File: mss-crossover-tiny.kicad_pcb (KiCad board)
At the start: 2 copper layers, 68.8 x 51 mm, 38 parts, among them J1 RJ45, J2 RJ45, J3 2x-screw, J4 2x-screw, J5 2x-screw, J6 ISP (5V), J7 2x-screw, Q1 2N3904, Q2 2N3904, SW1 Set, U1 L78M05CDT, U3 ATtiny25-20SS, U5 INA180A3

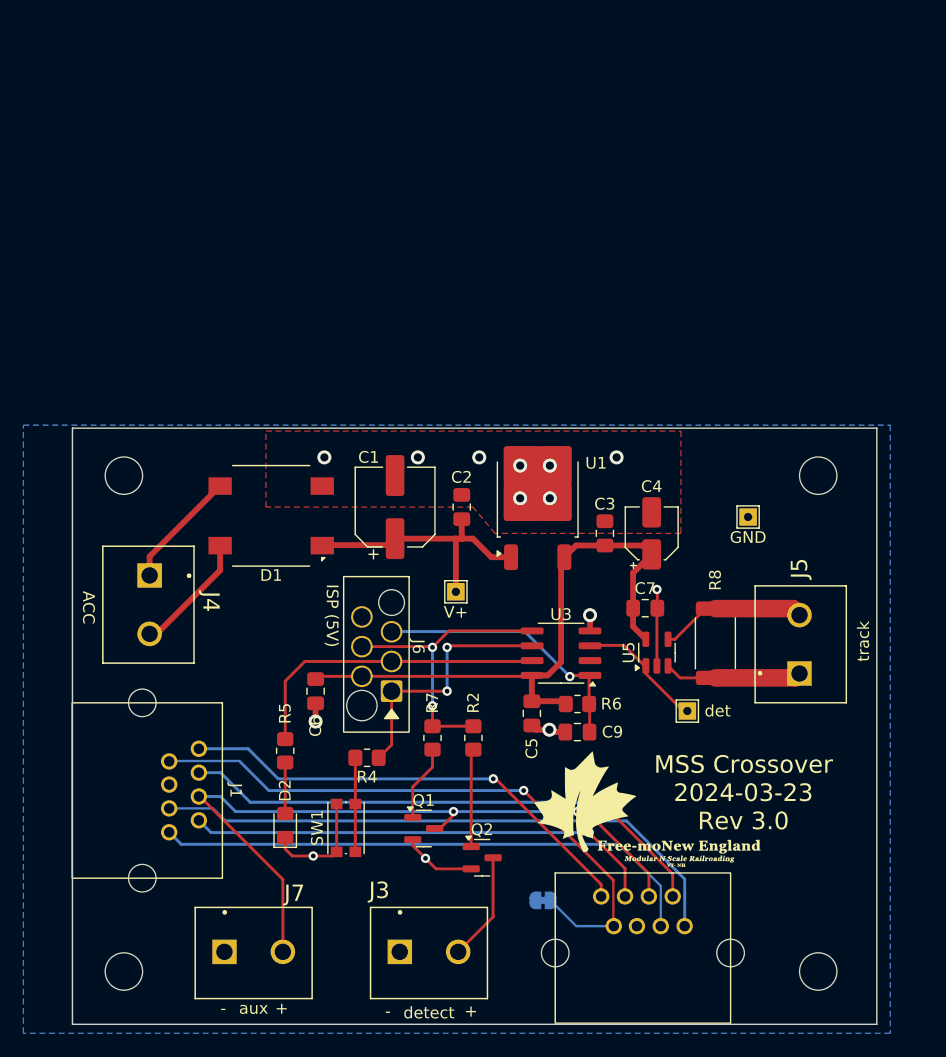
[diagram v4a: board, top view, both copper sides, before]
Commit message: Still working on then redesign for a resistive sense element.  Also added optoisolators.
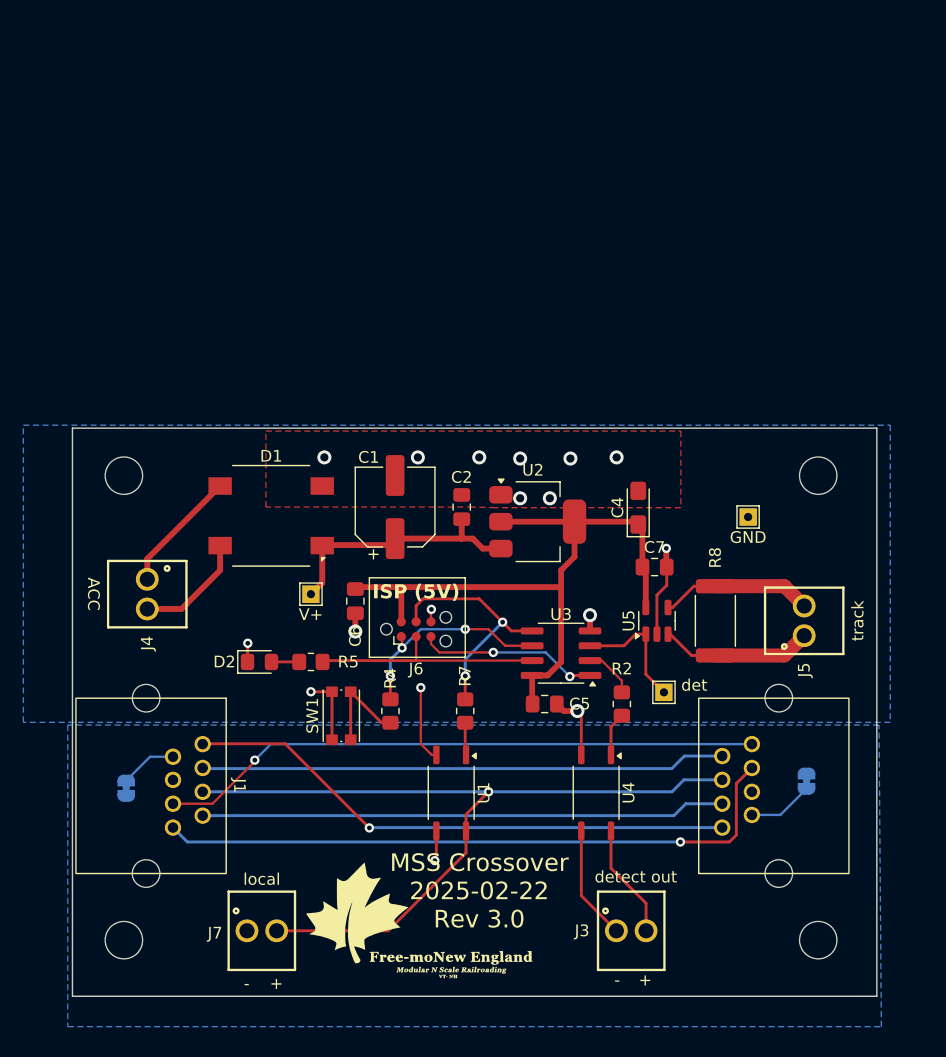
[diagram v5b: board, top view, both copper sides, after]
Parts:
- removed C3: 100nF, Capacitor_SMD:C_0805_2012Metric_Pad1.18x1.45mm_HandSolder
- removed C9: 1uF, Capacitor_SMD:C_0805_2012Metric_Pad1.18x1.45mm_HandSolder
- removed Q1, Q2: 2N3904, Package_TO_SOT_SMD:SOT-23
- removed R6: 10k, Resistor_SMD:R_0805_2012Metric_Pad1.20x1.40mm_HandSolder
- added JP2: MSS 7, Jumper:SolderJumper-2_P1.3mm_Bridged_RoundedPad1.0x1.5mm, B.Cu at (166.0, 120.2)
- added U2: AMS1117-3.3, Package_TO_SOT_SMD:SOT-223-3_TabPin2, F.Cu at (143.0, 98.0)
- added U4: TLP187, Package_SO:SOIC-4_4.55x3.7mm_P2.54mm, F.Cu at (148.0, 121.2)
- C4: value 10µF -> 22 µF; footprint Capacitor_SMD:CP_Elec_4x5.7 -> Capacitor_Tantalum_SMD:CP_EIA-3216-18_Kemet-A_Pad1.58x1.35mm_HandSolder
- D1: value DF04S-T -> DF04S
- J3, J4, J5, J7: value 2x-screw -> Screw_Terminal_01x02; footprint Imports:CUI_TB003-500-P02BE -> Imports:691210910002
- J6: value ISP (5V) -> ISP (5V); footprint myMods:skedd-6-debugging -> Connector:Tag-Connect_TC2030-IDC-NL_2x03_P1.27mm_Vertical
- R8: value 0.1 3W -> 0.1Ω
- U1: value L78M05CDT -> TLP187; footprint Package_TO_SOT_SMD:TO-252-2 -> Package_SO:SOIC-4_4.55x3.7mm_P2.54mm
- moved JP1 36.9 mm to (107.8, 120.8), turned to 90 degrees
- moved U1 26.3 mm to (135.6, 121.2), turned to -90 degrees
- moved G*** 21.7 mm to (132.8, 132.4)
- moved J3 19.9 mm to (151.0, 133.0)
- moved J2 15.2 mm to (161.3, 120.6), turned to 90 degrees
- moved D2 14.2 mm to (119.2, 110.0), turned to 0 degrees
- moved R2 13.0 mm to (150.2, 113.6)
- moved TP3 12.4 mm to (123.6, 104.2)
- moved SW1 9.61 mm to (126.2, 114.6)
- moved C6 8.42 mm to (127.4, 104.8)
- moved R5 7.91 mm to (123.6, 110.0), turned to 180 degrees
- moved J6 5.70 mm to (132.6, 107.2), turned to 0 degrees
- moved J5 4.53 mm to (165.8, 106.5)
- moved R4 4.47 mm to (130.4, 114.2), turned to -90 degrees
- moved J7 3.67 mm to (119.4, 133.0)
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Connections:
- J1 pad 5: GND -> /MSS GND
- J2 pad 5: GND -> /MSS GND
- J2 pad 7: /7 A -> /7 B
- J3 pad 1: GND -> Net-(J3-Pin_1)
- J7 pad 1: GND -> /MSS GND
- JP1 pad 1: GND -> /MSS GND
- R2 pad 1: /MOSI -> Net-(U3-XTAL1/PB3)
- R7 pad 2: Net-(Q1-B) -> Net-(R7-Pad2)
- U1 pad 1: Net-(D1-+) -> Net-(R7-Pad2)
- U1 pad 3: +5V -> GND
- U3 pad 2: unconnected-(U3-XTAL1/PB3-Pad2) -> Net-(U3-XTAL1/PB3)
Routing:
- net /7 A: track 52.5 -> 4.84 mm, vias 1 -> 0
- net Net-(J3-Pin_1): track 0.00 -> 9.79 mm
- net /RST: track 23.5 -> 15.4 mm, vias 1 -> 2
- net /AAin A: track 47.4 -> 55.2 mm, vias 0 -> 1
- net /Local A: track 62.0 -> 69.8 mm, vias 2 -> 1
- net /AD A: track 40.2 -> 47.5 mm
- net /SCK: track 26.8 -> 20.0 mm
- net Net-(Q1-B): track 6.50 -> 0.00 mm
- net +5V: track 52.0 -> 58.3 mm
- net /7 B: track 0.00 -> 5.60 mm
- net /MOSI: track 25.4 -> 20.6 mm
- net Net-(R2-Pad2): track 8.38 -> 3.74 mm
- net Net-(U3-XTAL1/PB3): track 0.00 -> 4.44 mm
- net /Ain A: track 40.6 -> 44.9 mm, vias 1 -> 0
- net /MISO: track 22.0 -> 18.2 mm, vias 2 -> 3
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- added copper zone on B.Cu, net /MSS GND
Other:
- board size 68.8 x 51 mm -> 68.8 x 48.6 mm

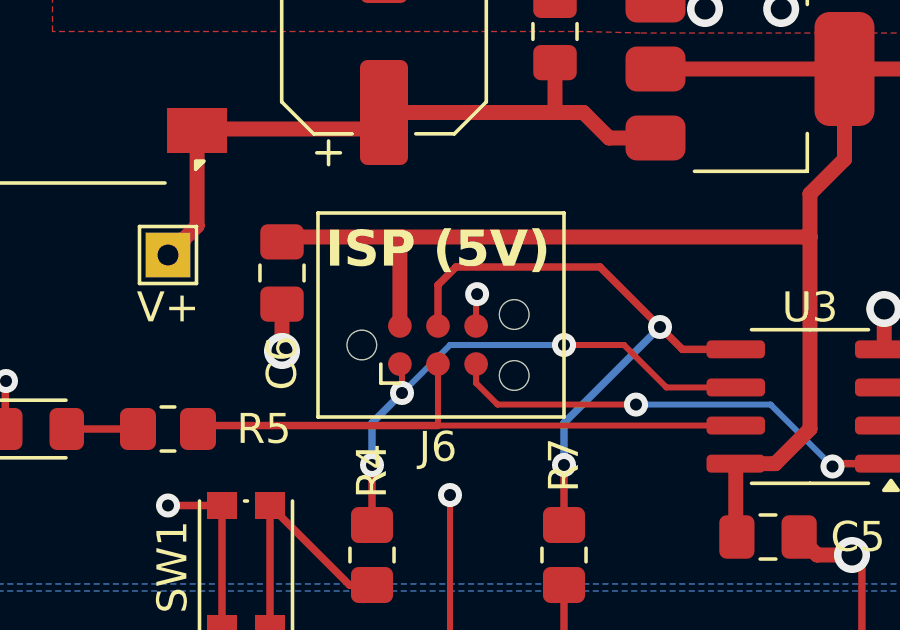
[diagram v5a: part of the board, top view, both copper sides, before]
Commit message: Changed everything to 3.3V instead of 5V
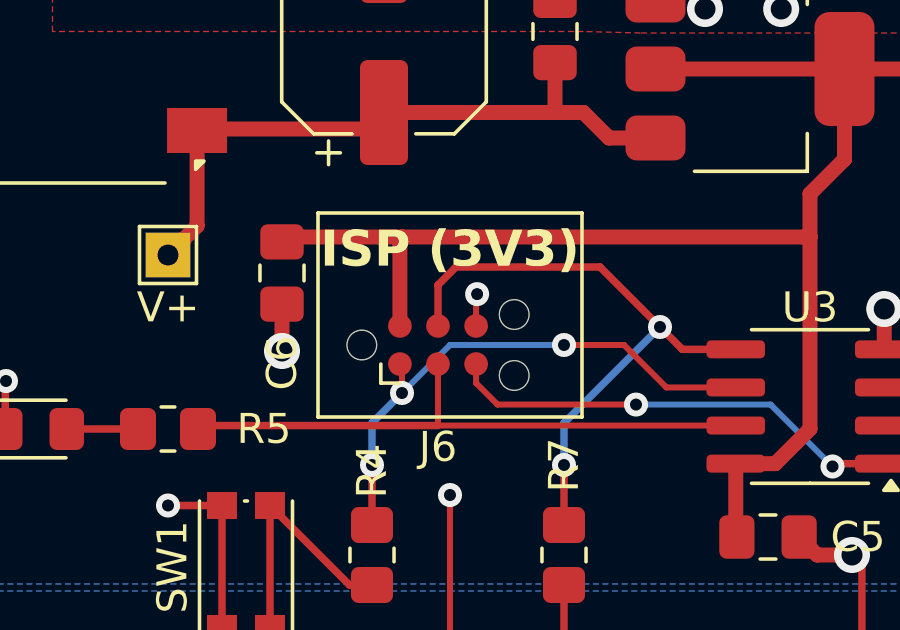
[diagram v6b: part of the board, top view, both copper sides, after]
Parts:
- J6: value ISP (5V) -> ISP (3V3)
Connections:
- net +5V renamed +3.3V
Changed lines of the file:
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@@
 	(net 4 "Net-(D1-+)")
 	(net 5 "/AD A")
-	(net 6 "+5V")
+	(net 6 "+3.3V")
 	(net 7 "GND")
 	(net 8 "/Ain B")
@@
 			(layers "F.Cu" "F.Paste" "F.Mask")
 			(roundrect_rratio 0.25)
-			(net 6 "+5V")
+			(net 6 "+3.3V")
 			(pinfunction "VO")
 			(pintype "power_out")
@@
 			(layers "F.Cu" "F.Paste" "F.Mask")
 			(roundrect_rratio 0.25)
-			(net 6 "+5V")
+			(net 6 "+3.3V")
 			(pinfunction "VO")
 			(pintype "power_out")
@@
 			(layers "F.Cu" "F.Paste" "F.Mask")
 			(roundrect_rratio 0.25)
-			(net 6 "+5V")
+			(net 6 "+3.3V")
 			(pinfunction "VCC")
 			(pintype "power_in")
@@
 			(layers "F.Cu" "F.Paste" "F.Mask")
 			(roundrect_rratio 0.25)
-			(net 6 "+5V")
+			(net 6 "+3.3V")
 			(pinfunction "V+")
 			(pintype "power_in")
@@
 			(layers "F.Cu" "F.Paste" "F.Mask")
 			(roundrect_rratio 0.2127659574)
-			(net 6 "+5V")
+			(net 6 "+3.3V")
 			(pintype "passive")
 		)
@@
 			(layers "F.Cu" "F.Paste" "F.Mask")
 			(roundrect_rratio 0.2127659574)
-			(net 6 "+5V")
+			(net 6 "+3.3V")
 			(pintype "passive")
 		)
@@
 			(layers "F.Cu" "F.Paste" "F.Mask")
 			(roundrect_rratio 0.185185)
-			(net 6 "+5V")
+			(net 6 "+3.3V")
 			(pintype "passive")
 		)
@@
 			)
 		)
-		(property "Value" "ISP (5V)"
-			(at 0 -3.2 0)
+		(property "Value" "ISP (3V3)"
+			(at 0.4 -3.2 0)
 			(layer "F.SilkS")
 			(effects
@@
 			(size 0.7874 0.7874)
 			(layers "F.Cu" "F.Mask")
-			(net 6 "+5V")
+			(net 6 "+3.3V")
 			(pinfunction "Pin_2")
 			(pintype "passive")
@@
 			(layers "F.Cu" "F.Paste" "F.Mask")
 			(roundrect_rratio 0.2127659574)
-			(net 6 "+5V")
+			(net 6 "+3.3V")
 			(pintype "passive")
 		)
@@
 	(gr_rect
 		(start 128.6 102.8)
-		(end 136.8 109.6)
+		(end 137.4 109.6)
 		(stroke
 			(width 0.12)

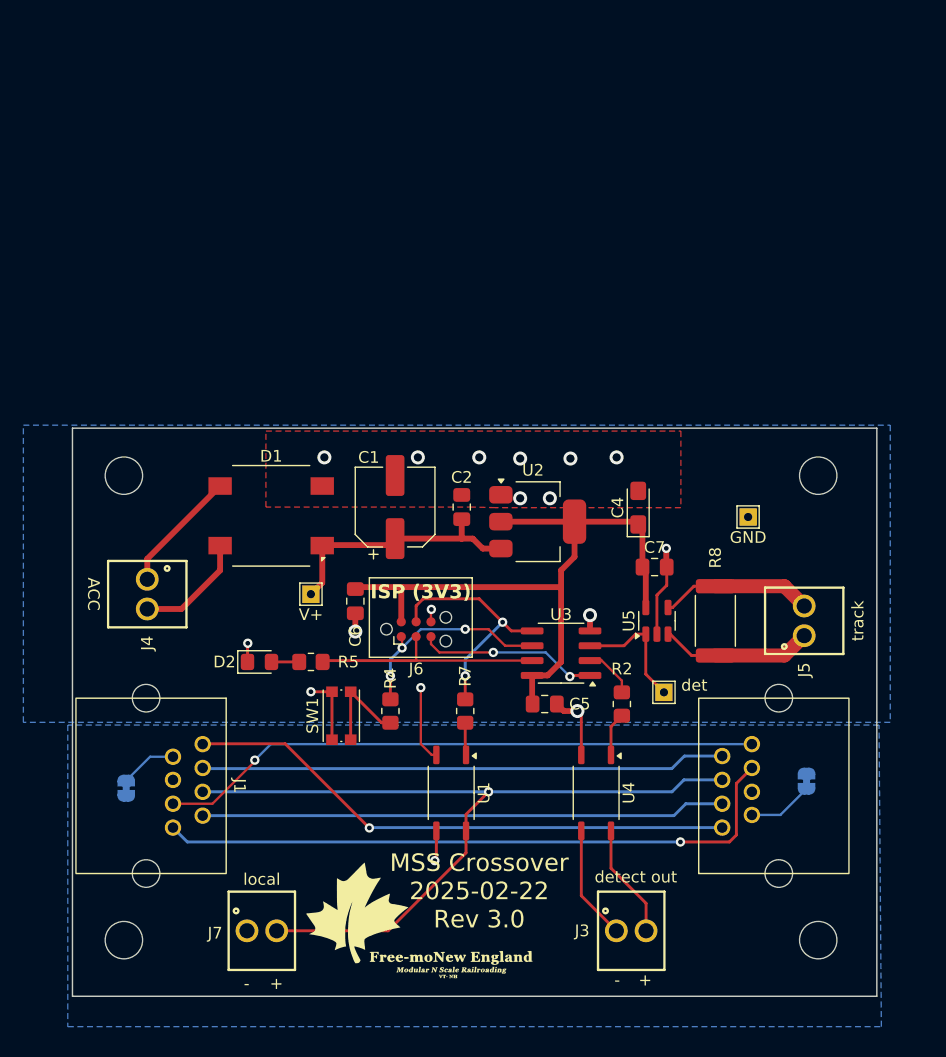
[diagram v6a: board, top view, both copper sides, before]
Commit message: Updated to KiCad v9.  This is the release that was sent to JLCPCB for assembly as version 4.0.
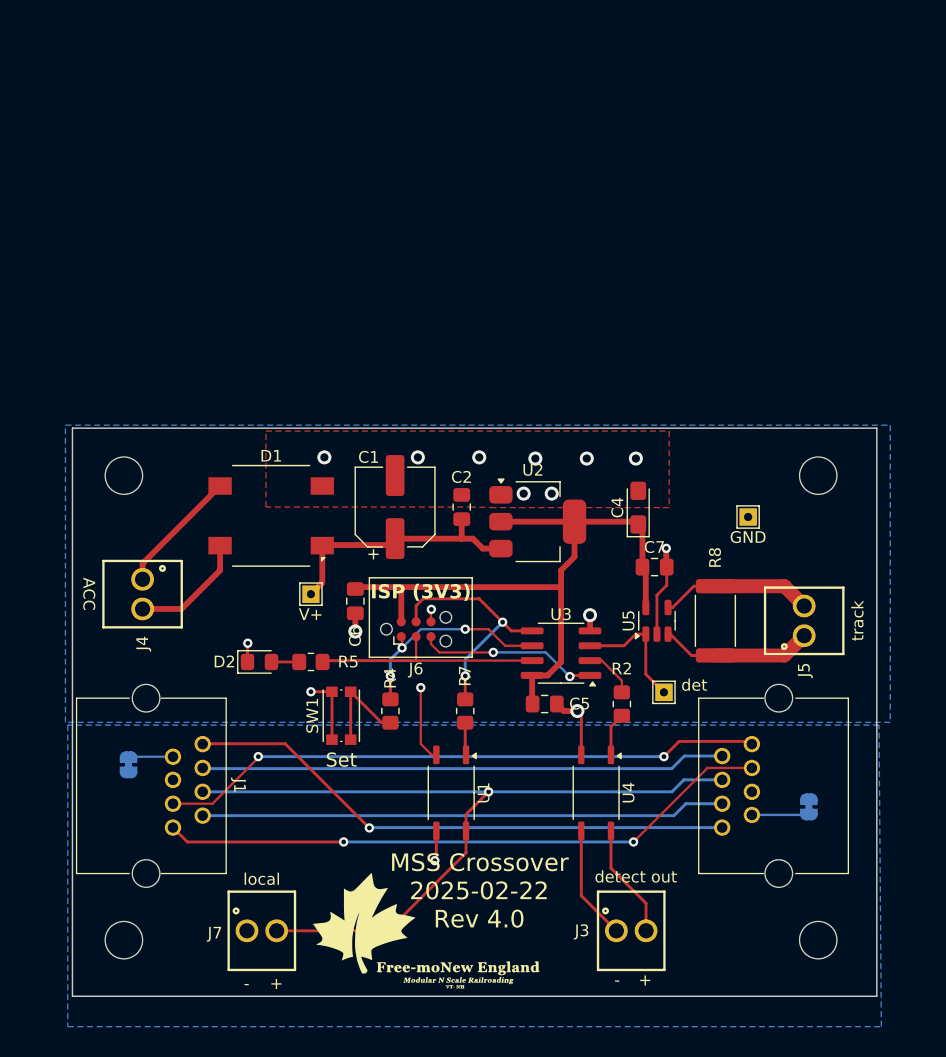
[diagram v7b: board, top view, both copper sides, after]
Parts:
- moved JP2 2.21 mm to (166.2, 122.4)
- moved JP1 2.01 mm to (108.0, 118.8)
- moved G*** 1.07 mm to (133.4, 133.3)
- moved J4 0.40 mm to (109.2, 104.2)
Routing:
- net /AAin A: track 55.2 -> 52.7 mm, vias 1 -> 2
- net /7 A: track 4.84 -> 3.82 mm
- net /7 B: track 5.60 -> 4.89 mm
- net /AAin B: track 51.7 -> 51.9 mm, vias 1 -> 2

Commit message: Some small changes learned from the first prototype.  Switch back to the larger screw terminals and changed resistor to the pushbutton to 2.2k instead of 4.7k.
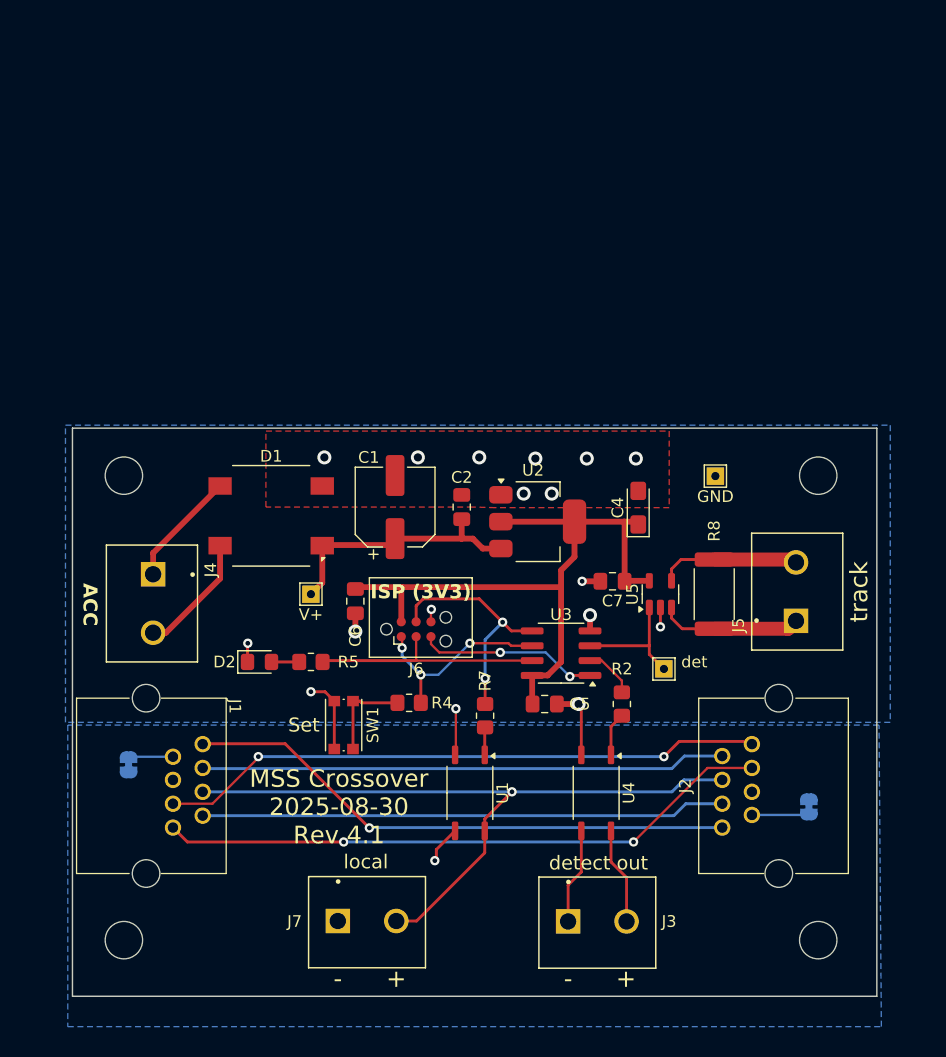
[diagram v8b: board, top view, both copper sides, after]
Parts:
- G***: moved to B.Cu
- J3, J4, J5, J7: footprint Imports:691210910002 -> Imports:CUI_TB003-500-P02BE
- R4: value 4.7k -> 2.2k
- moved G*** 12.7 mm to (140.9, 123.0), turned to 180 degrees
- moved J7 6.55 mm to (125.9, 132.2)
- moved J3 5.46 mm to (145.6, 132.2)
- moved TP1 4.48 mm to (158.2, 94.1)
- moved C7 3.80 mm to (149.4, 103.1), turned to 180 degrees
- moved U5 2.30 mm to (153.5, 104.2)
- moved R8 2.29 mm to (158.1, 104.2)
- moved TP2 2.00 mm to (153.8, 110.6)
- moved J4 1.92 mm to (110.1, 102.5)
- moved R4 1.75 mm to (132.0, 113.5), turned to 180 degrees
- moved R7 1.75 mm to (138.5, 114.6)
- moved U1 1.60 mm to (137.2, 121.2)
- moved SW1 0.82 mm to (126.4, 115.4)
- moved J5 0.70 mm to (165.1, 106.5)
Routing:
- net /Local A: track 69.8 -> 61.0 mm
- net GND: track 31.6 -> 25.5 mm, vias 16 -> 17
- net Net-(J3-Pin_1): track 9.79 -> 8.22 mm
- net Net-(J3-Pin_2): track 9.79 -> 8.30 mm
- net /MISO: track 18.2 -> 17.1 mm
- net Net-(J5-Pin_2): track 13.1 -> 12.1 mm
- net Net-(J5-Pin_1): track 13.1 -> 12.2 mm
- net Net-(J4-Pin_1): track 10.7 -> 9.92 mm
- net /MSS GND: track 2.60 -> 3.27 mm
- net Net-(R4-Pad2): track 8.60 -> 7.96 mm
